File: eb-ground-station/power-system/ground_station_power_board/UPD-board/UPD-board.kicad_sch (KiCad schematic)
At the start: 82 parts

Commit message: New power board schematic almost done
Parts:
- added C? (x3): 0.1uf, symbol Device:C
- added R? (x2): 4k7, symbol Device:R
- added U?: UA78M33, symbol Regulator_Linear:uA7805
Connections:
- net +12V: now also C?.1, U?.1 (IN)
- net +3V3: now also C?.1, R?.1, R?.1
- net GND: now also C?.2, C?.2, C?.2, U?.2 (GND)
- net RX2: now also R?.2
- net TX2: now also R?.2
- new net +3.3V: C?.1, U?.3 (OUT)
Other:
- note added: "3.3V 1A regulator"
- note added: "Connectors"
- note added: "ICs"
- note added: "Populate these to use UART2 as I2C0"
- note added: "Power / Indicators"
- note added: "Pull Resistors"
- note added: "also i2c0"
- note added: "console"
- note added: "i2c1"
- moved on the sheet: C?, D?, FB?, J?, JP?, R?, RN?, U?

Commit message: First layout done. No slikscreen work yet
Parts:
- added H1, H2, H3, H4: MountingHole, oresat-footprints:H-MCMASTER-94100A150, symbol Mechanical:MountingHole
- C1: renamed from C; footprint (none) -> Capacitor_SMD:C_0603_1608Metric; DPN (none) -> 1276-1935-2-ND; MPN (none) -> CL10B104KB8NNWC; Mfr (none) -> Samsung Electro-Mechanics
- C10, C11: renamed from C?; footprint (none) -> Capacitor_SMD:CP_Elec_6.3x5.9; DPN (none) -> 732-8438-2-ND; MPN (none) -> 865080445010; Mfr (none) -> Würth Elektronik
- C2, C3, C4, C5, C6, C9: renamed from C?; footprint (none) -> Capacitor_SMD:C_0603_1608Metric; DPN (none) -> 1276-1935-2-ND; MPN (none) -> CL10B104KB8NNWC; Mfr (none) -> Samsung Electro-Mechanics
- C7, C8: renamed from C?; value 0.1u -> 0.1uf; footprint (none) -> Capacitor_SMD:C_0603_1608Metric; DPN (none) -> 1276-1935-2-ND; MPN (none) -> CL10B104KB8NNWC; Mfr (none) -> Samsung Electro-Mechanics
- D1, D10, D11, D12, D13, D14, D15, D16, D17, D18, D19, D2, D20, D21, D22, D23, D24, D25, D26, D3, D4, D5, D6, D7, D8, D9: renamed from D?; footprint (none) -> LED_SMD:LED_0603_1608Metric
- FB1, FB2: renamed from FB?; footprint (none) -> Capacitor_SMD:C_1206_3216Metric
- J1: renamed from J?; footprint (none) -> Connector_PinHeader_2.54mm:PinHeader_1x04_P2.54mm_Vertical
- J10, J9: renamed from J?; value Conn_01x08 -> PI 1827486; footprint (none) -> Connector_Phoenix_MC:PhoenixContact_MC_1,5_8-GF-3.81_1x08_P3.81mm_Horizontal_ThreadedFlange_MountHole
- J2: renamed from J?; footprint (none) -> Connector_Phoenix_MC_HighVoltage:PhoenixContact_MC_1,5_3-GF-5.08_1x03_P5.08mm_Horizontal_ThreadedFlange_MountHole
- J3, J4, J5, J6: renamed from J?; footprint (none) -> Connector_PinHeader_2.54mm:PinHeader_1x06_P2.54mm_Vertical
- J7, J8: renamed from J?; value Conn_01x08 -> PI 1809131; footprint (none) -> Connector_Phoenix_MC_HighVoltage:PhoenixContact_MC_1,5_8-GF-5.08_1x08_P5.08mm_Horizontal_ThreadedFlange_MountHole
- JP1, JP10, JP11, JP12, JP13, JP2, JP3, JP4, JP5, JP6, JP7, JP8, JP9: renamed from JP?; value SolderJumper -> SolderJumper3; footprint (none) -> Jumper:SolderJumper-3_P1.3mm_Bridged12_Pad1.0x1.5mm
- R1, R2, R3, R4, R5: renamed from R?; footprint (none) -> Resistor_SMD:R_0603_1608Metric
- R6: renamed from R?; value R -> 1500; footprint (none) -> Resistor_SMD:R_0603_1608Metric
- R7: renamed from R?; value R -> 620; footprint (none) -> Resistor_SMD:R_0603_1608Metric
- RN1, RN10, RN11, RN12, RN2, RN3, RN4, RN5, RN6, RN7, RN8, RN9: renamed from RN?; footprint (none) -> Resistor_SMD:R_Array_Convex_4x0603
- U1, U2, U3: renamed from U?; footprint (none) -> Package_SO:TSSOP-16_4.4x5mm_P0.65mm
- U4: renamed from U?; footprint (none) -> Package_SO:MSOP-8_3x3mm_P0.65mm
- U6: renamed from U?; footprint (none) -> Package_TO_SOT_SMD:SOT-223-3_TabPin2
- U7: renamed from U?; footprint (none) -> Connector_IDC:IDC-Header_2x20_P2.54mm_Vertical
- gave numbers to parts that had none: 1
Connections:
- net +3.3V is gone; now on net +3V3: C9.1, U6.3 (OUT)
- net ADC_RDY: now also U7.13 (GPIO27)
- net GND: no longer U7. (GND)
- net TMP_ALERT: now also U7.11 (GPIO17)
- net ~{IO_RESET}: now also U7.37 (GPIO26)
- now unconnected: U7.1 (+3.3V), U7.17 (+3.3V), U7.2 (+5.0V), U7.4 (+5.0V)
- no-connect marks 26 -> 25
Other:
- moved on the sheet: J1, J3, J4, J5, J6

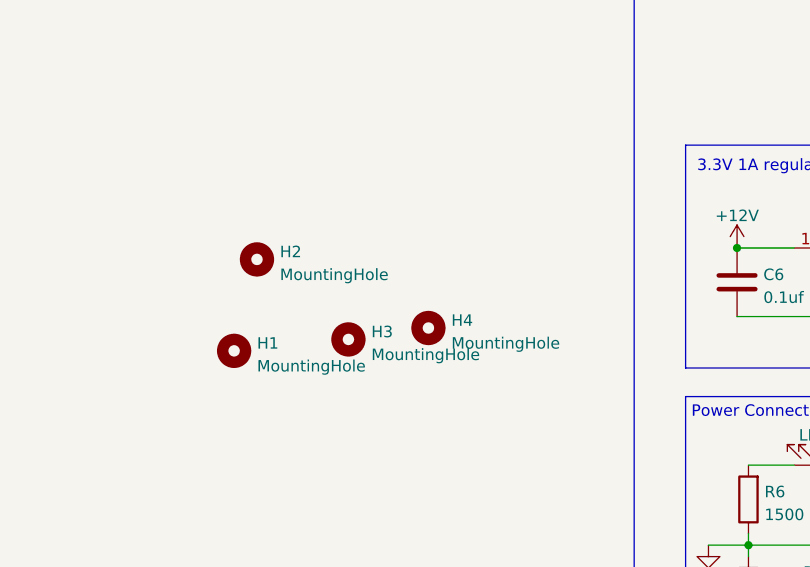
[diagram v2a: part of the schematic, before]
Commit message: Added PDF schematic
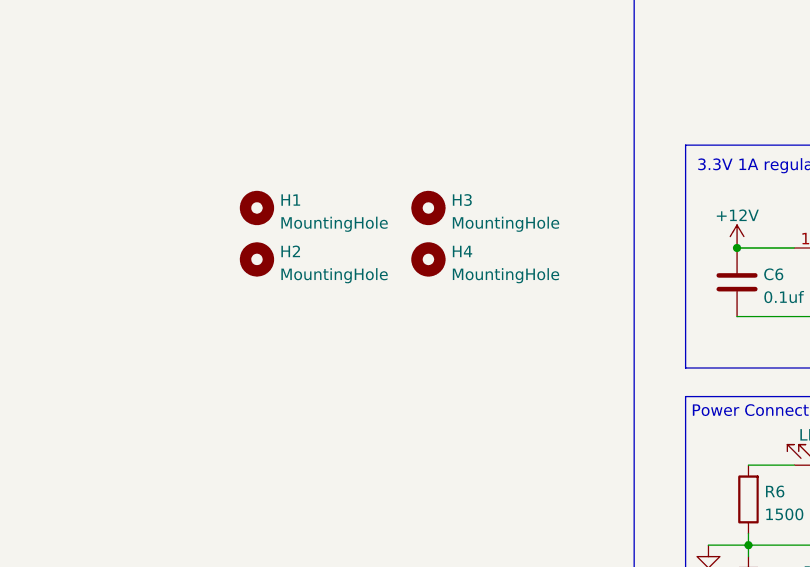
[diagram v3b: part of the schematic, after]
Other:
- moved on the sheet: H1, H3, H4
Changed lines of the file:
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@@
     (pin "1")
   )
-  (symbol (lib_id "Mechanical:MountingHole") (at 199.39 227.33 0) (unit 1)
-    (in_bom yes) (on_board yes) (fields_autoplaced)
-    (property "Reference" "H4" (id 0) (at 201.93 226.4953 0)
-      (effects (font (size 1.27 1.27)) (justify left))
-    )
-    (property "Value" "MountingHole" (id 1) (at 201.93 229.0322 0)
-      (effects (font (size 1.27 1.27)) (justify left))
-    )
-    (property "Footprint" "oresat-footprints:H-MCMASTER-94100A150" (id 2) (at 199.39 227.33 0)
-      (effects (font (size 1.27 1.27)) hide)
-    )
-    (property "Datasheet" "~" (id 3) (at 199.39 227.33 0)
+  (symbol (lib_id "Mechanical:MountingHole") (at 199.39 219.71 0) (unit 1)
+    (in_bom yes) (on_board yes) (fields_autoplaced)
+    (property "Reference" "H4" (id 0) (at 201.93 218.8753 0)
+      (effects (font (size 1.27 1.27)) (justify left))
+    )
+    (property "Value" "MountingHole" (id 1) (at 201.93 221.4122 0)
+      (effects (font (size 1.27 1.27)) (justify left))
+    )
+    (property "Footprint" "oresat-footprints:H-MCMASTER-94100A150" (id 2) (at 199.39 219.71 0)
+      (effects (font (size 1.27 1.27)) hide)
+    )
+    (property "Datasheet" "~" (id 3) (at 199.39 219.71 0)
       (effects (font (size 1.27 1.27)) hide)
     )
@@
     (pin "8")
   )
-  (symbol (lib_id "Mechanical:MountingHole") (at 177.8 229.87 0) (unit 1)
-    (in_bom yes) (on_board yes) (fields_autoplaced)
-    (property "Reference" "H1" (id 0) (at 180.34 229.0353 0)
-      (effects (font (size 1.27 1.27)) (justify left))
-    )
-    (property "Value" "MountingHole" (id 1) (at 180.34 231.5722 0)
-      (effects (font (size 1.27 1.27)) (justify left))
-    )
-    (property "Footprint" "oresat-footprints:H-MCMASTER-94100A150" (id 2) (at 177.8 229.87 0)
-      (effects (font (size 1.27 1.27)) hide)
-    )
-    (property "Datasheet" "~" (id 3) (at 177.8 229.87 0)
+  (symbol (lib_id "Mechanical:MountingHole") (at 180.34 213.995 0) (unit 1)
+    (in_bom yes) (on_board yes) (fields_autoplaced)
+    (property "Reference" "H1" (id 0) (at 182.88 213.1603 0)
+      (effects (font (size 1.27 1.27)) (justify left))
+    )
+    (property "Value" "MountingHole" (id 1) (at 182.88 215.6972 0)
+      (effects (font (size 1.27 1.27)) (justify left))
+    )
+    (property "Footprint" "oresat-footprints:H-MCMASTER-94100A150" (id 2) (at 180.34 213.995 0)
+      (effects (font (size 1.27 1.27)) hide)
+    )
+    (property "Datasheet" "~" (id 3) (at 180.34 213.995 0)
       (effects (font (size 1.27 1.27)) hide)
     )
@@
     (pin "1")
   )
-  (symbol (lib_id "Mechanical:MountingHole") (at 190.5 228.6 0) (unit 1)
-    (in_bom yes) (on_board yes) (fields_autoplaced)
-    (property "Reference" "H3" (id 0) (at 193.04 227.7653 0)
-      (effects (font (size 1.27 1.27)) (justify left))
-    )
-    (property "Value" "MountingHole" (id 1) (at 193.04 230.3022 0)
-      (effects (font (size 1.27 1.27)) (justify left))
-    )
-    (property "Footprint" "oresat-footprints:H-MCMASTER-94100A150" (id 2) (at 190.5 228.6 0)
-      (effects (font (size 1.27 1.27)) hide)
-    )
-    (property "Datasheet" "~" (id 3) (at 190.5 228.6 0)
-      (effects (font (size 1.27 1.27)) hide)
-    )
+  (symbol (lib_id "Mechanical:MountingHole") (at 199.39 213.995 0) (unit 1)
+    (in_bom yes) (on_board yes) (fields_autoplaced)
+    (property "Reference" "H3" (id 0) (at 201.93 213.1603 0)
+      (effects (font (size 1.27 1.27)) (justify left))
+    )
+    (property "Value" "MountingHole" (id 1) (at 201.93 215.6972 0)
+      (effects (font (size 1.27 1.27)) (justify left))
+    )
+    (property "Footprint" "oresat-footprints:H-MCMASTER-94100A150" (id 2) (at 199.39 213.995 0)
+      (effects (font (size 1.27 1.27)) hide)
+    )
+    (property "Datasheet" "~" (id 3) (at 199.39 213.995 0)
+      (effects (font (size 1.27 1.27)) hide)
+    )

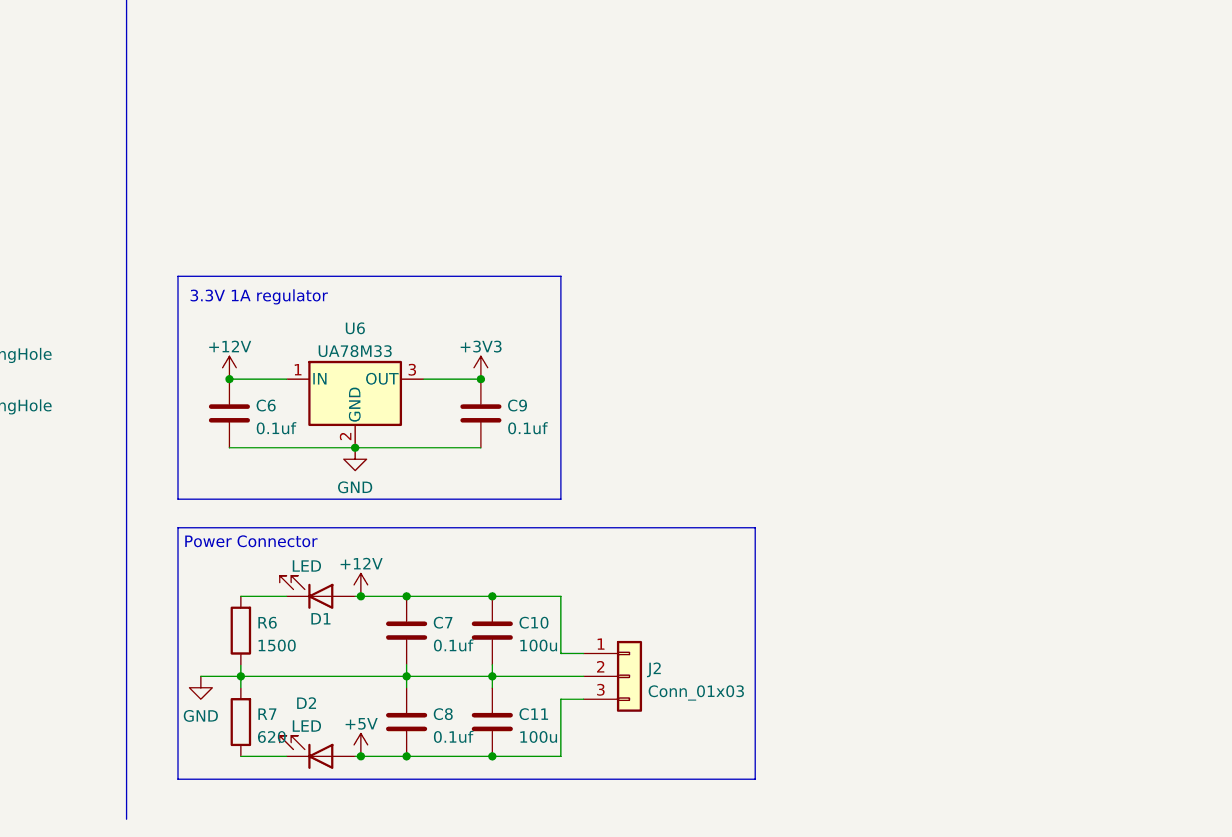
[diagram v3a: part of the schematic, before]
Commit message: Added soft start and ground vias
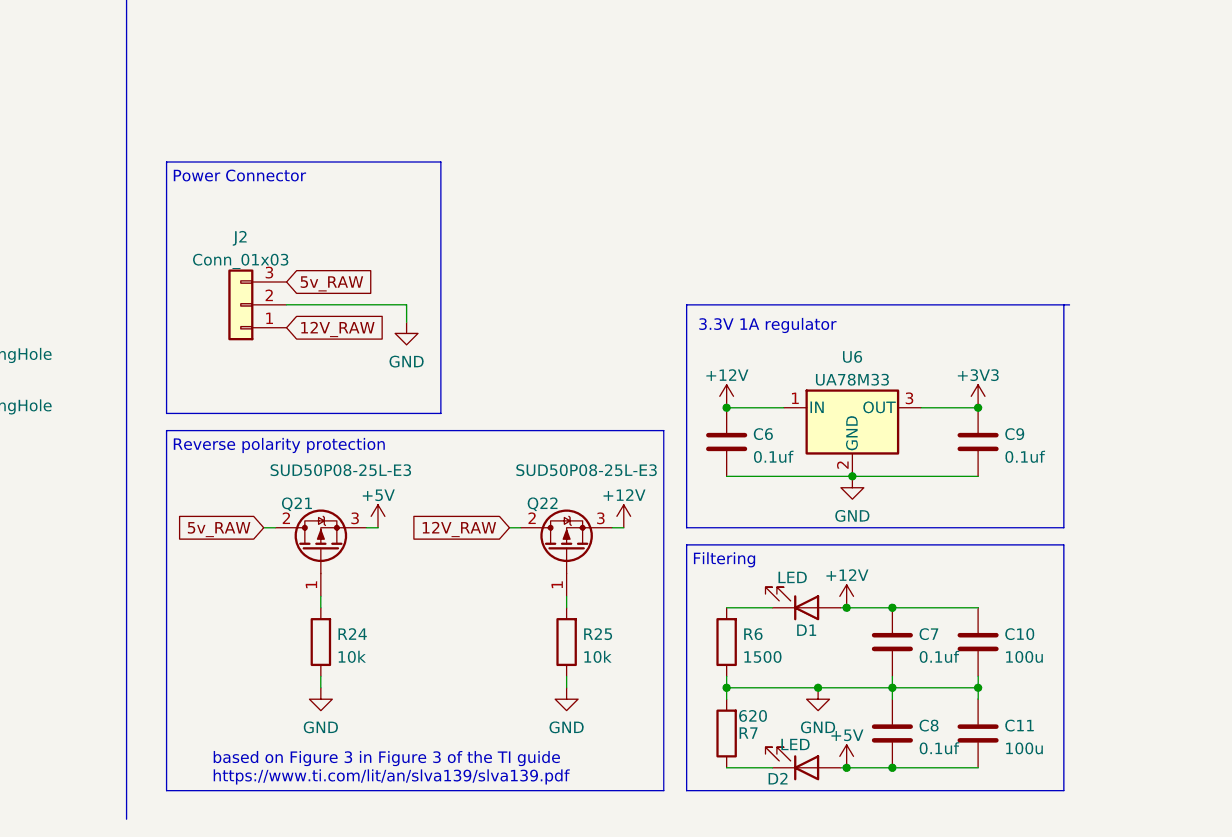
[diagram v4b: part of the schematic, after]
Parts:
- added Q21, Q22: SUD50P08-25L-E3, oresat-footprints:TO-252-3_TabIsPin2, symbol Device:Q_PMOS_GDS
- added R24, R25: 10k, Resistor_SMD:R_0603_1608Metric, symbol Device:R
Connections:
- net +12V: now also Q22.3 (S); no longer J2.1 (Pin_1)
- net +5V: now also Q21.3 (S); no longer J2.3 (Pin_3)
- net GND: now also R24.1, R25.1
- new net: Q22.1 (G), R25.2
- new net: Q21.1 (G), R24.2
- new net 12V_RAW: J2.1 (Pin_1), Q22.2 (D)
- new net 5v_RAW: J2.3 (Pin_3), Q21.2 (D)
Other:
- note added: "Filtering"
- note added: "Reverse polarity protection"
- note added: "based on Figure 3 in Figure 3 of the TI guide https://www.ti.com/lit/an/slva139/slva139.pdf"
- moved on the sheet: C10, C11, C6, C7, C8, C9, D1, D2, J2, R6, R7, U6

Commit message: refdes silkscreen nearly done
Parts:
- FB1, FB2: footprint Capacitor_SMD:C_1206_3216Metric -> oresat-footprints:1206-or-0805
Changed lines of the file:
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@@
     (property "Reference" "FB2" (id 0) (at 146.685 73.025 90))
     (property "Value" "FerriteBead" (id 1) (at 145.415 77.47 90))
-    (property "Footprint" "Capacitor_SMD:C_1206_3216Metric" (id 2) (at 149.225 76.073 90)
+    (property "Footprint" "oresat-footprints:1206-or-0805" (id 2) (at 149.225 76.073 90)
       (effects (font (size 1.27 1.27)) hide)
     )
@@
     (property "Reference" "FB1" (id 0) (at 146.685 50.165 90))
     (property "Value" "FerriteBead" (id 1) (at 149.225 54.61 90))
-    (property "Footprint" "Capacitor_SMD:C_1206_3216Metric" (id 2) (at 149.225 53.213 90)
+    (property "Footprint" "oresat-footprints:1206-or-0805" (id 2) (at 149.225 53.213 90)
       (effects (font (size 1.27 1.27)) hide)
     )
@@
     )
     (path "/fb76027d-7de7-4547-9f04-dd609d7e0ba6"
-      (reference "FB1") (unit 1) (value "FerriteBead") (footprint "Capacitor_SMD:C_1206_3216Metric")
+      (reference "FB1") (unit 1) (value "FerriteBead") (footprint "oresat-footprints:1206-or-0805")
     )
     (path "/70be2267-34be-40e9-aef3-2acfb73f4b41"
-      (reference "FB2") (unit 1) (value "FerriteBead") (footprint "Capacitor_SMD:C_1206_3216Metric")
+      (reference "FB2") (unit 1) (value "FerriteBead") (footprint "oresat-footprints:1206-or-0805")
     )
     (path "/8ae10509-281c-4962-a6b9-e66ad947c9fb"

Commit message: More silkscreen work
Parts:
- C10, C11: symbol Device:C -> Device:C_Polarized
- J10, J9: footprint Connector_Phoenix_MC:PhoenixContact_MC_1,5_8-GF-3.81_1x08_P3.81mm_Horizontal_ThreadedFlange_MountHole -> oresat-footprints:J_PhoenixContact_MC_1,5_8-GF-3.81_1x08_P3.81mm_45degree_ThreadedFlange
- J7: footprint Connector_Phoenix_MC_HighVoltage:PhoenixContact_MC_1,5_8-GF-5.08_1x08_P5.08mm_Horizontal_ThreadedFlange_MountHole -> oresat-footprints:J_PhoenixContact_MC_1,5_8-GF-5.08_1x08_P5.08mm_Horizontal_ThreadedFlange
- J8: value PI 1809131 -> PI 1827923; footprint Connector_Phoenix_MC_HighVoltage:PhoenixContact_MC_1,5_8-GF-5.08_1x08_P5.08mm_Horizontal_ThreadedFlange_MountHole -> Connector_Phoenix_MC:PhoenixContact_MC_1,5_8-GF-3.81_1x08_P3.81mm_Horizontal_ThreadedFlange
- JP1, JP10, JP11, JP12, JP13, JP2, JP3, JP4, JP5, JP6, JP7, JP8, JP9: footprint Jumper:SolderJumper-3_P1.3mm_Bridged12_Pad1.0x1.5mm -> oresat-footprints:SolderJumper-3_P1.3mm_Bridged12_Pad1.0x1.5mm
- U1, U2, U3: footprint Package_SO:TSSOP-16_4.4x5mm_P0.65mm -> oresat-footprints:TSSOP-16_4.4x5mm_P0.65mm
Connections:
- net +5V: now also C11.1; no longer C11.2
- net GND: now also C11.2; no longer C11.1

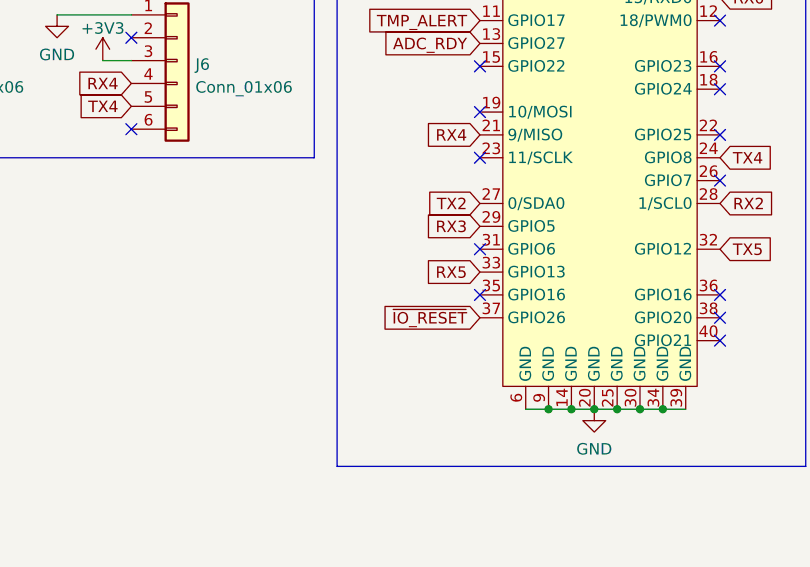
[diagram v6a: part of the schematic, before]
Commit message: Fixed ~IO_RESET RasPi pin and improved silkscreen
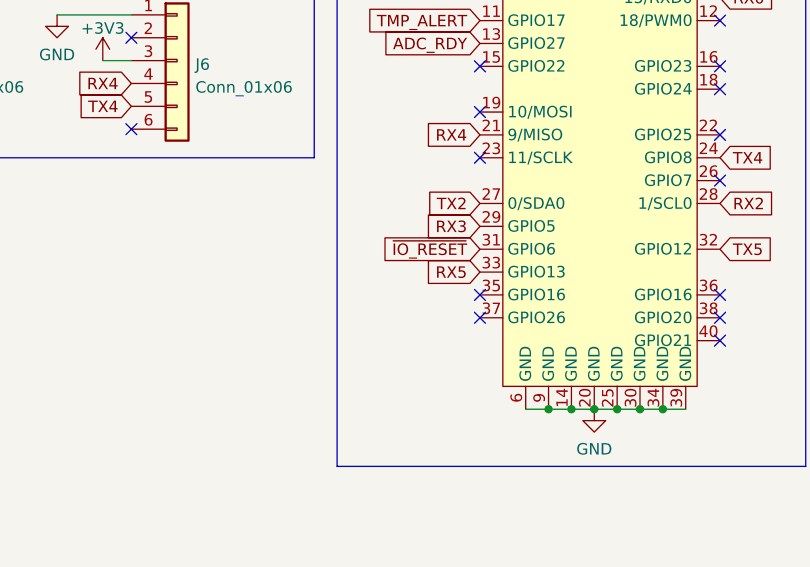
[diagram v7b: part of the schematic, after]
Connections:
- net ~{IO_RESET}: now also U7.31 (GPIO6); no longer U7.37 (GPIO26)
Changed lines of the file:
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@@
   (no_connect (at 365.76 68.58))
   (no_connect (at 339.09 53.34))
-  (no_connect (at 339.09 63.5))
+  (no_connect (at 339.09 71.12))
   (no_connect (at 365.76 45.72))
   (no_connect (at 365.76 43.18))
@@
     )
   )
-  (global_label "~{IO_RESET}" (shape input) (at 339.09 71.12 180) (fields_autoplaced)
-    (effects (font (size 1.27 1.27)) (justify right))
-    (property "Intersheet References" "${INTERSHEET_REFS}" (id 0) (at 328.0288 71.1994 0)
-      (effects (font (size 1.27 1.27)) (justify right) hide)
-    )
+  (global_label "~{IO_RESET}" (shape input) (at 339.09 63.5 180) (fields_autoplaced)
+    (effects (font (size 1.27 1.27)) (justify right))
+    (property "Intersheet References" "${INTERSHEET_REFS}" (id 0) (at 328.0288 63.5794 0)
+      (effects (font (size 1.27 1.27)) (justify right) hide)
+    )
